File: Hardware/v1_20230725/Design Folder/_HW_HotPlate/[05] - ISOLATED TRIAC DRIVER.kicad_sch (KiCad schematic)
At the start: 10 parts, among them J501 TERM_3POS_5.08MM_SIDE, J502 TERM_3POS_5.08MM_SIDE, Q501 T2050H-6G-TR, U501 140817143400, U502 MOC3022S

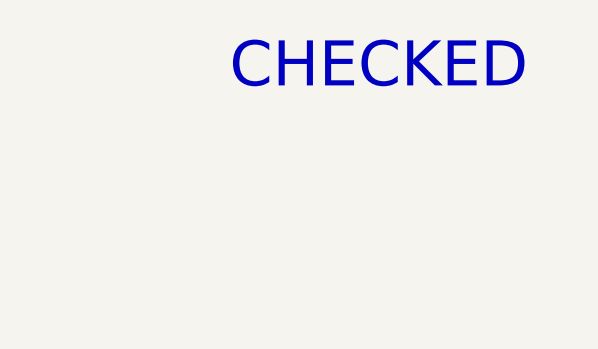
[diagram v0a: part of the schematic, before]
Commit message: Schematic library has been updated
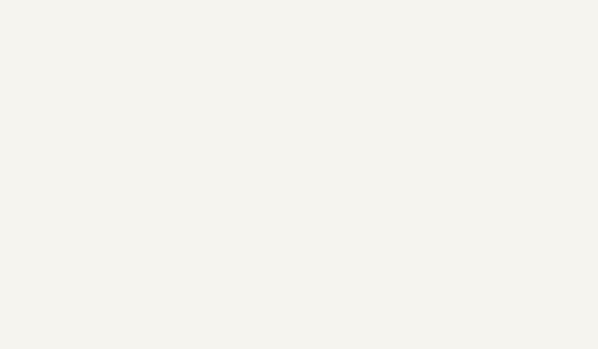
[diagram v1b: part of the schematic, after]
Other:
- note removed: "CHECKED"
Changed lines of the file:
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@@
 (kicad_sch (version 20230121) (generator eeschema)
-  (paper "B")
+  (paper "C")
   (title_block
     (title "Hot Plate")
@@
     (company "Mend0z0")
     (comment 1 "v1")
+    (comment 2 "RELEASED")
     (comment 3 "Siavash Taher Parvar")
     (comment 8 "N/A")
@@
     (effects (font (size 5.08 5.08)) (justify left bottom))
   )
-  (text "CHECKED" (at 378.46 36.83 0)
-    (effects (font (size 5 5)) (justify left bottom))
-  )
   (text "DESIGN NOTE:\n\nThe Idea for finding the zero-crossing\npoint is by capturing the positive peeks\nvalue and then derive the zero point\n\nIMPORTANT: \nOpto Ion = 1mA, Von = 0.9V, V Rectifier diode = 0.7V\nVon : (0.001A * 100KR) + 0.9 + 0.7 ~= +110V\n\nIt's possible to figure out the frequency and\nworking voltage by the delay between two +110V."

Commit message: components have been updated
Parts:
- D501: symbol _SCHLIB_HotPlate:DIODE_S1J_600V_1A_SMA -> _SCHLIB_HotPlate:DIODE_GP_S1J_600V_1A_SMA; Manufacturer (none) -> SMC Diode Solutions; PCB CHECk (none) -> PCB (N/A); Part Number S1J -> (none); Part Number (Manufacturer) (none) -> S1J; Part Number (Vendor) (none) -> 1655-S1JTR-ND; SCH CHECK CHECKED -> SCH (N/A); Vendor (none) -> Digikey
- J501, J502: value TERM_3POS_5.08MM_SIDE -> TERM_3POS_SIDE_5.08MM; symbol _SCHLIB_HotPlate:TERM_3POS_5.08MM_SIDE -> _SCHLIB_HotPlate:CONN_TERM_3POS_SIDE_5.08MM; Manufacturer (none) -> Adam Tech; PCB CHECk (none) -> PCB (N/A); Package (none) -> THD_SIDE; Part Number EB147A-03-D -> (none); Part Number (Manufacturer) (none) -> EB147A-03-D; Part Number (Vendor) (none) -> 2057-EB147A-03-D-ND; SCH CHECK CHECKED -> SCH (N/A); Vendor (none) -> Digikey
- Q501: value T2050H-6G-TR -> T2050H-6G-TR_600V_20A; symbol _SCHLIB_HotPlate:Q_T2050H-6G-TR -> _SCHLIB_HotPlate:Q_TRIAC_T2050H-6G-TR_600V_20A_D2PAK; Manufacturer (none) -> STMicroelectronics; PCB CHECk (none) -> PCB (N/A); Part Number T2050H-6G-TR -> (none); Part Number (Manufacturer) (none) -> T2050H-6G-TR; Part Number (Vendor) (none) -> 497-17285-2-ND; SCH CHECK CHECKED -> SCH (N/A); Vendor (none) -> Digikey
- R501: value 10KR_1/20W -> 10KR_1/20W_1%; symbol _SCHLIB_HotPlate:RES_10KR_1/20W-R0201 -> _SCHLIB_HotPlate:RES_10KR_1/20W_1%_R0201; Manufacturer (none) -> Stackpole Electronics Inc; PCB CHECk (none) -> PCB (N/A); Part Number RMCF0201FT10K0 -> (none); Part Number (Manufacturer) (none) -> RMCF0201FT10K0; Part Number (Vendor) (none) -> RMCF0201FT10K0TR-ND; SCH CHECK CHECKED -> SCH (N/A); Vendor (none) -> Digikey
- R502: value 100KR_1W -> 100KR_1W_1%; symbol _SCHLIB_HotPlate:RES_100KR_1W_MELF -> _SCHLIB_HotPlate:RES_100KR_1W_1%_MELF; Manufacturer (none) -> Vishay Beyschlag/Draloric/BC Components; PCB CHECk (none) -> PCB (N/A); Part Number SMM02070C1003FBP00 -> (none); Part Number (Manufacturer) (none) -> SMM02070C1003FBP00; Part Number (Vendor) (none) -> 749-1134-2-ND; SCH CHECK CHECKED -> SCH (N/A); Vendor (none) -> Digikey
- R503: value 3KR_2W -> 3KR_2W_1%; symbol _SCHLIB_HotPlate:RES_3KR_2W_R2512 -> _SCHLIB_HotPlate:RES_3KR_2W_1%_R2512; Manufacturer (none) -> TE Connectivity Passive Product; PCB CHECk (none) -> PCB (N/A); Part Number 35213K0FT -> (none); Part Number (Manufacturer) (none) -> 35213K0FT; Part Number (Vendor) (none) -> A116043TR-ND; SCH CHECK * -> SCH (N/A); Vendor (none) -> Digikey
- R504: value 330R_1/10W -> 330R_1/10W_1%; symbol _SCHLIB_HotPlate:RES_330R_1/10W-R0402 -> _SCHLIB_HotPlate:RES_330R_1/10W_1%_R0402; Manufacturer (none) -> Panasonic Electronic Components; PCB CHECk (none) -> PCB (N/A); Part Number ERJ-2RKF3300X -> (none); Part Number (Manufacturer) (none) -> ERJ-2RKF3300X; Part Number (Vendor) (none) -> P330LTR-ND; SCH CHECK CHECKED -> SCH (N/A); Vendor (none) -> Digikey
- U501: symbol _SCHLIB_HotPlate:ISOLATOR_140817143400_4-SMD -> _SCHLIB_HotPlate:IC_OPTOISOLATOR_140817143400_TRANSISTOR_5kV_35V_0.05A_4-SMD Gull Wing; Manufacturer (none) -> Würth Elektronik; PCB CHECk (none) -> PCB (N/A); Package (none) -> 4-SMD Gull Wing; Part Number 140817143400 -> (none); Part Number (Manufacturer) (none) -> 140817143400; Part Number (Vendor) (none) -> 732-140817143400TR-ND; SCH CHECK CHECKED -> SCH (N/A); Vendor (none) -> Digikey
- U502: symbol _SCHLIB_HotPlate:ISOLATOR_MOC3022S -> _SCHLIB_HotPlate:IC_OPTOISOLATOR_MOC3022S_TRIAC_5kV_400V_6-SMD, Gull Wing; Manufacturer (none) -> Lite-On Inc.; PCB CHECk (none) -> PCB (N/A); Package (none) -> 6-SMD, Gull Wing; Part Number MOC3022S -> (none); Part Number (Manufacturer) (none) -> MOC3022S; Part Number (Vendor) (none) -> 160-1377-5-ND; SCH CHECK CHECKED -> SCH (N/A); Vendor (none) -> Digikey
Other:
- moved on the sheet: D501, J501, J502, Q501, R501, R502, R503, R504, U501, U502

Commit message: Updating hardware format structure
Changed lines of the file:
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@@
     (stroke (width 0) (type default))
   )
-  (polyline (pts (xy 309.88 196.85) (xy 367.03 196.85))
+  (polyline (pts (xy 326.39 196.85) (xy 384.81 196.85))
     (stroke (width 0) (type default))
   )
@@
     (stroke (width 0.508) (type dot))
   )
-  (polyline (pts (xy 311.15 193.04) (xy 313.69 193.04))
+  (polyline (pts (xy 327.66 193.04) (xy 330.2 193.04))
     (stroke (width 0) (type default))
   )
@@
     (stroke (width 0) (type default))
   )
-  (polyline (pts (xy 309.88 187.96) (xy 367.03 187.96))
+  (polyline (pts (xy 326.39 187.96) (xy 384.81 187.96))
     (stroke (width 0) (type default))
   )
@@
     (stroke (width 0) (type default))
   )
-  (polyline (pts (xy 367.03 196.85) (xy 367.03 187.96))
+  (polyline (pts (xy 384.81 196.85) (xy 384.81 187.96))
     (stroke (width 0) (type default))
   )
@@
     (stroke (width 0) (type default) (color 255 29 154 1))
   )
-  (polyline (pts (xy 311.15 193.04) (xy 312.42 190.5))
+  (polyline (pts (xy 327.66 193.04) (xy 328.93 190.5))
     (stroke (width 0) (type default))
   )
@@
     (stroke (width 0) (type default))
   )
-  (polyline (pts (xy 313.69 193.04) (xy 312.42 190.5))
+  (polyline (pts (xy 330.2 193.04) (xy 328.93 190.5))
     (stroke (width 0) (type default))
   )
@@
     (stroke (width 0) (type default))
   )
-  (polyline (pts (xy 309.88 187.96) (xy 309.88 196.85))
+  (polyline (pts (xy 326.39 187.96) (xy 326.39 196.85))
     (stroke (width 0) (type default))
   )
@@
   )
   (text "10mA  @ 30 Vac\n50mA @ 150 Vac\n70mA @ 210 Vac (not very compatible with 240 Vac)"
-    (at 314.96 195.58 0)
-    (effects (font (size 1.27 1.27)) (justify left bottom))
-  )
+    (at 331.47 195.58 0)
+    (effects (font (size 1.27 1.27)) (justify left bottom))
+  )
